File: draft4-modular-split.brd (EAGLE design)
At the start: 100 x 88 mm, 34 parts, among them U2 SPX3819, X1 3v7 lipo, X2 ESP-12, X3 MOD-TP4056

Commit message: make all caps consistent footprints
split VSYS into two forks to distribute power better.  even at 1mm wide,
trace resistance is estimted at 300mOhm.  (but that's for the whole
lenght, not longest fork)
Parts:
- C21, C22: value 10µF -> 10uF
- C23: device microbuilder:0603-NO -> microbuilder:0805-NO
- C3, C31, C4, C5: device microbuilder:_0805 -> microbuilder:0805-NO
- moved C23 0.14 mm to (12.2, 18.2)
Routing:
- net VSYS: track 196.2 -> 256.8 mm, vias 2 -> 3
- net GND: track 48.8 -> 38.3 mm
- net D5_IN: track 45.8 -> 47.3 mm

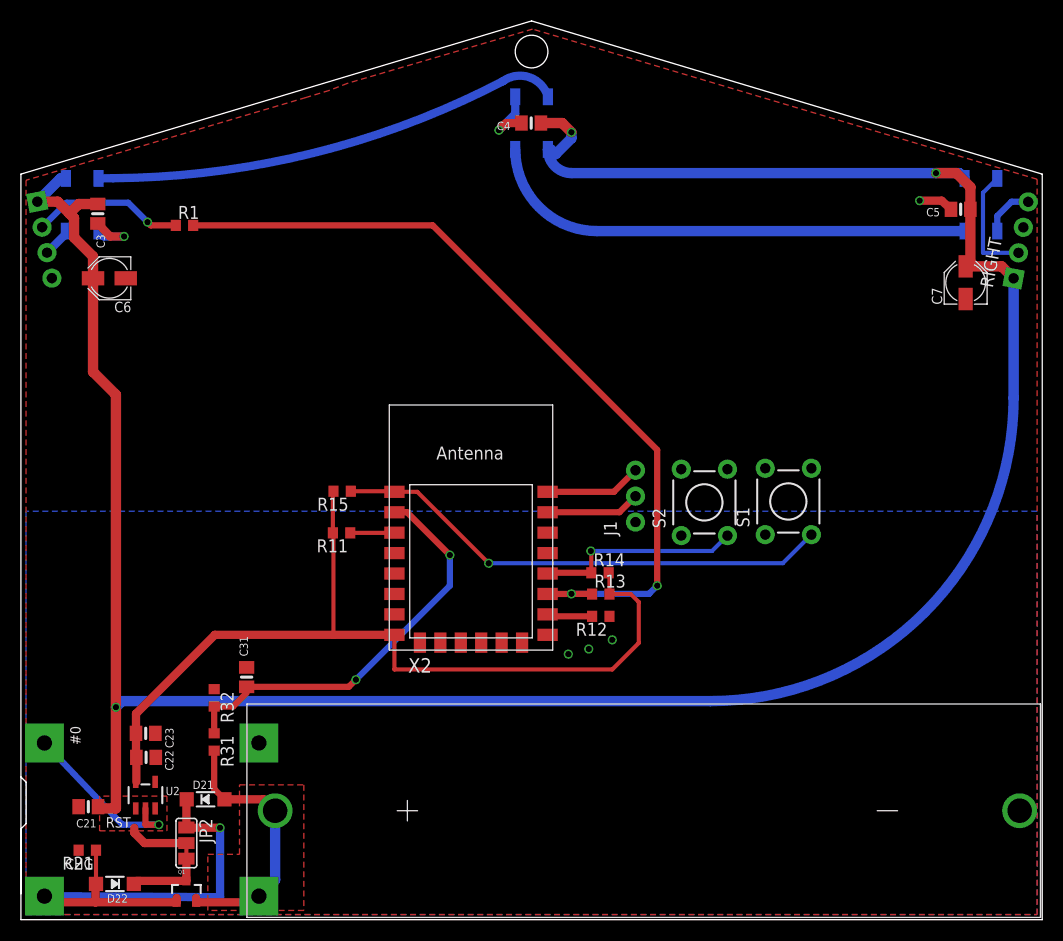
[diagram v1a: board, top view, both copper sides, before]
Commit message: smash and fix all silk
Add notes on connectors and test points
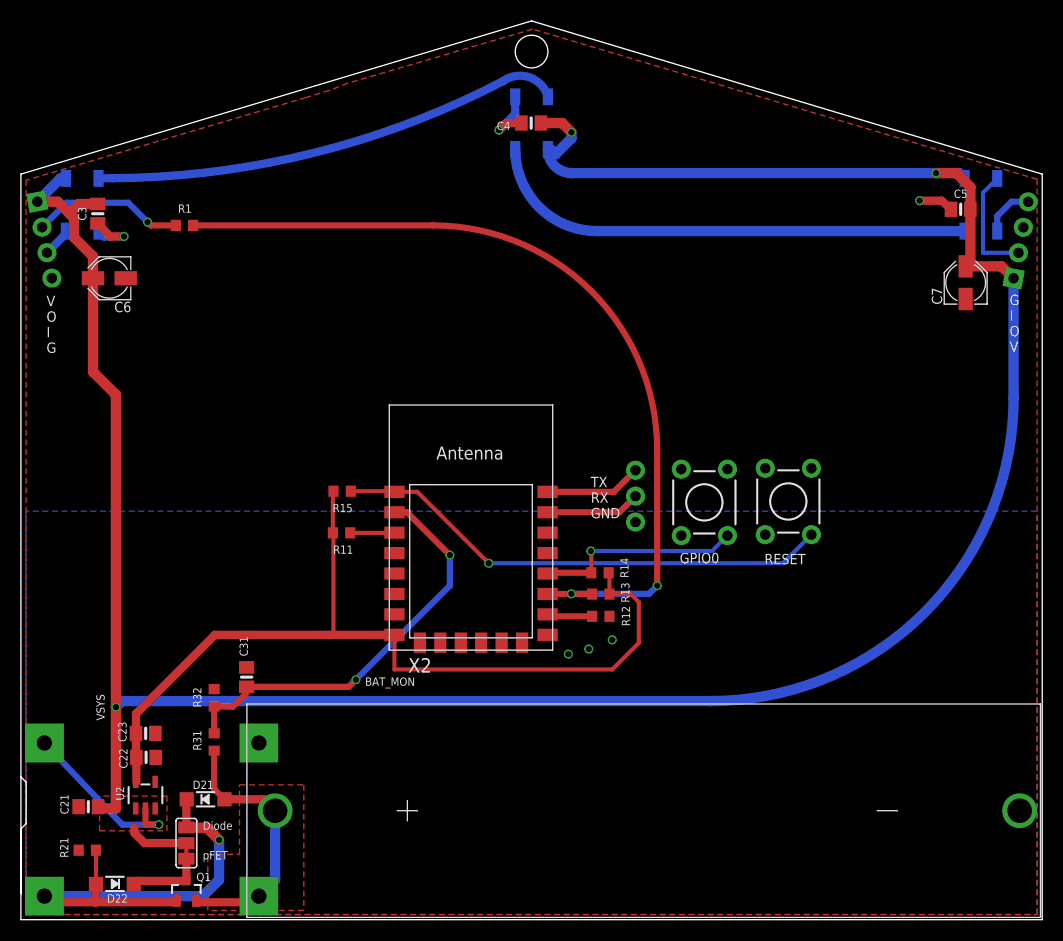
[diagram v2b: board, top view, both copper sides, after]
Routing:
- net VBUS: track 48.8 -> 46.9 mm
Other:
- board text added: "BAT_MON"
- board text added: "Diode"
- board text added: "G I O V"
- board text added: "GPIO0"
- board text added: "RESET"
- board text added: "TX RX GND"
- board text added: "V O I G"
- board text added: "VSYS"
- board text added: "pFET"
- board text removed: "#0"
- board text removed: "CHG"
- board text removed: "RST"
